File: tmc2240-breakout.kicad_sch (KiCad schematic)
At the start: 91 parts, among them J1 Conn_01x06, J2 Conn_01x05, J3 Conn_01x02, J4 Conn_01x02, J5 Conn_01x15, J6 Conn_01x06, J7 Conn_01x05, Q10 2N7002, Q11 2N7002, Q12 2N7002, Q13 2N7002, Q14 2N7002, Q2 2N7002, Q3 2N7002, Q5 2N7002, Q6 2N7002, Q7 2N7002, Q8 2N7002, Q9 2N7002, U1 TMC2240ATJ+, U2 LD1117S18TR_SOT223

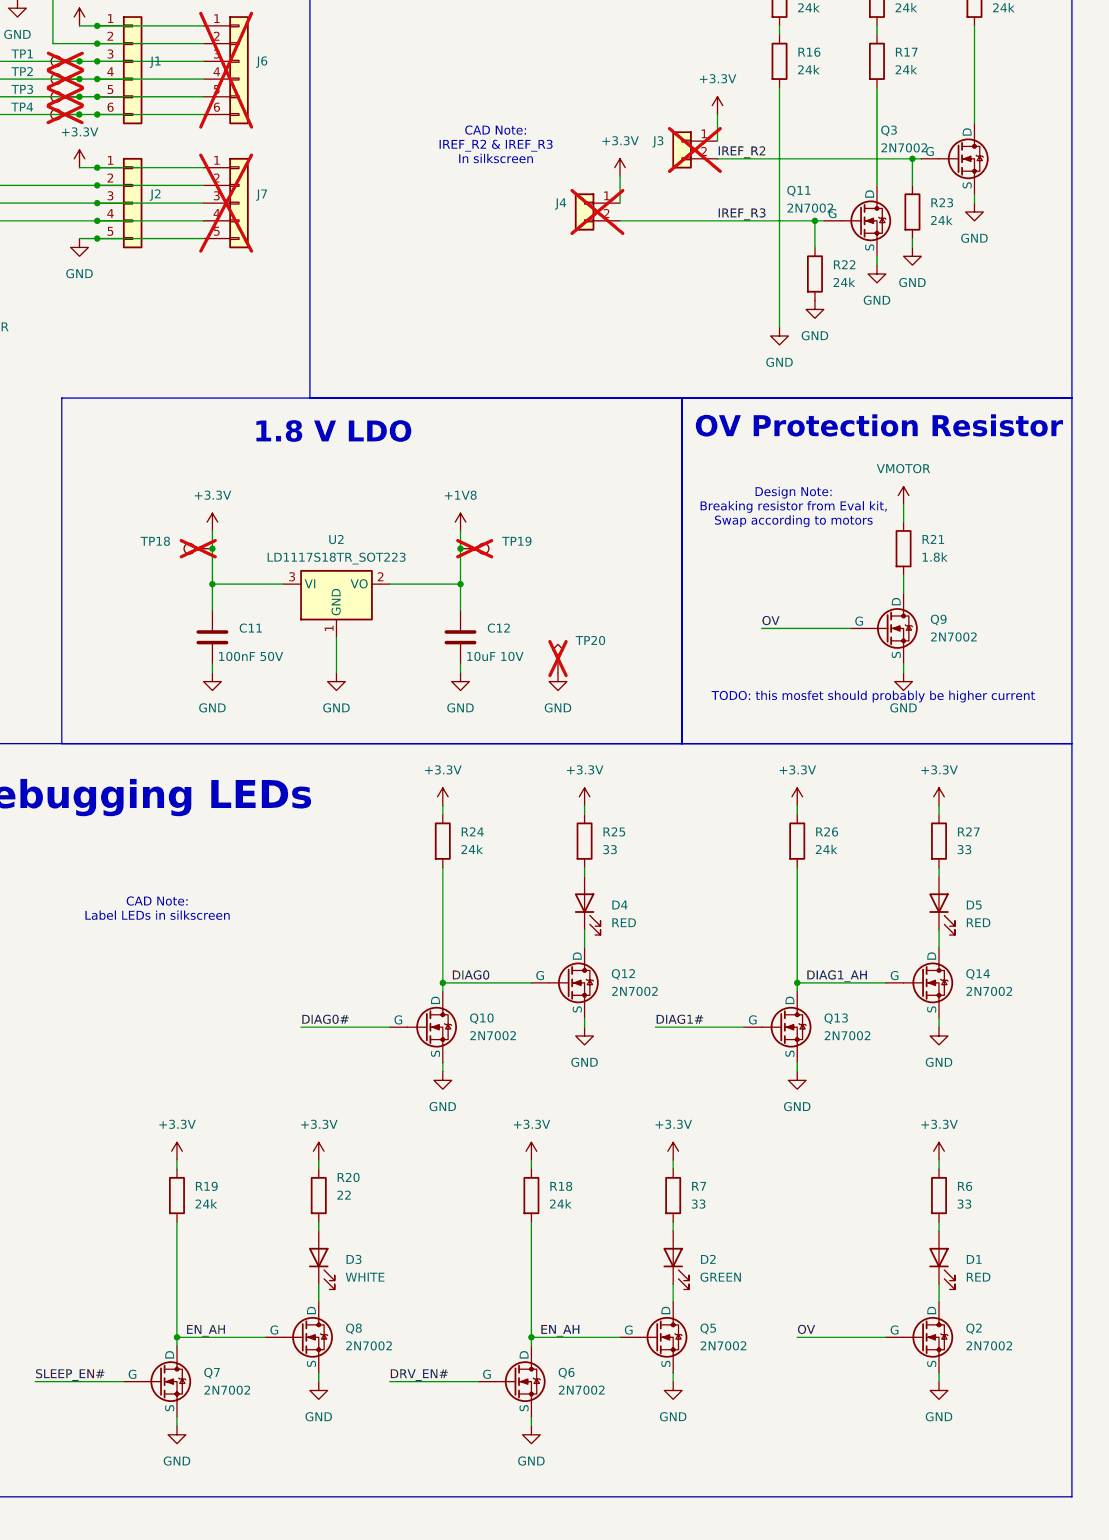
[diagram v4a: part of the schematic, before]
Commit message: did more sourcing and fixed footprints
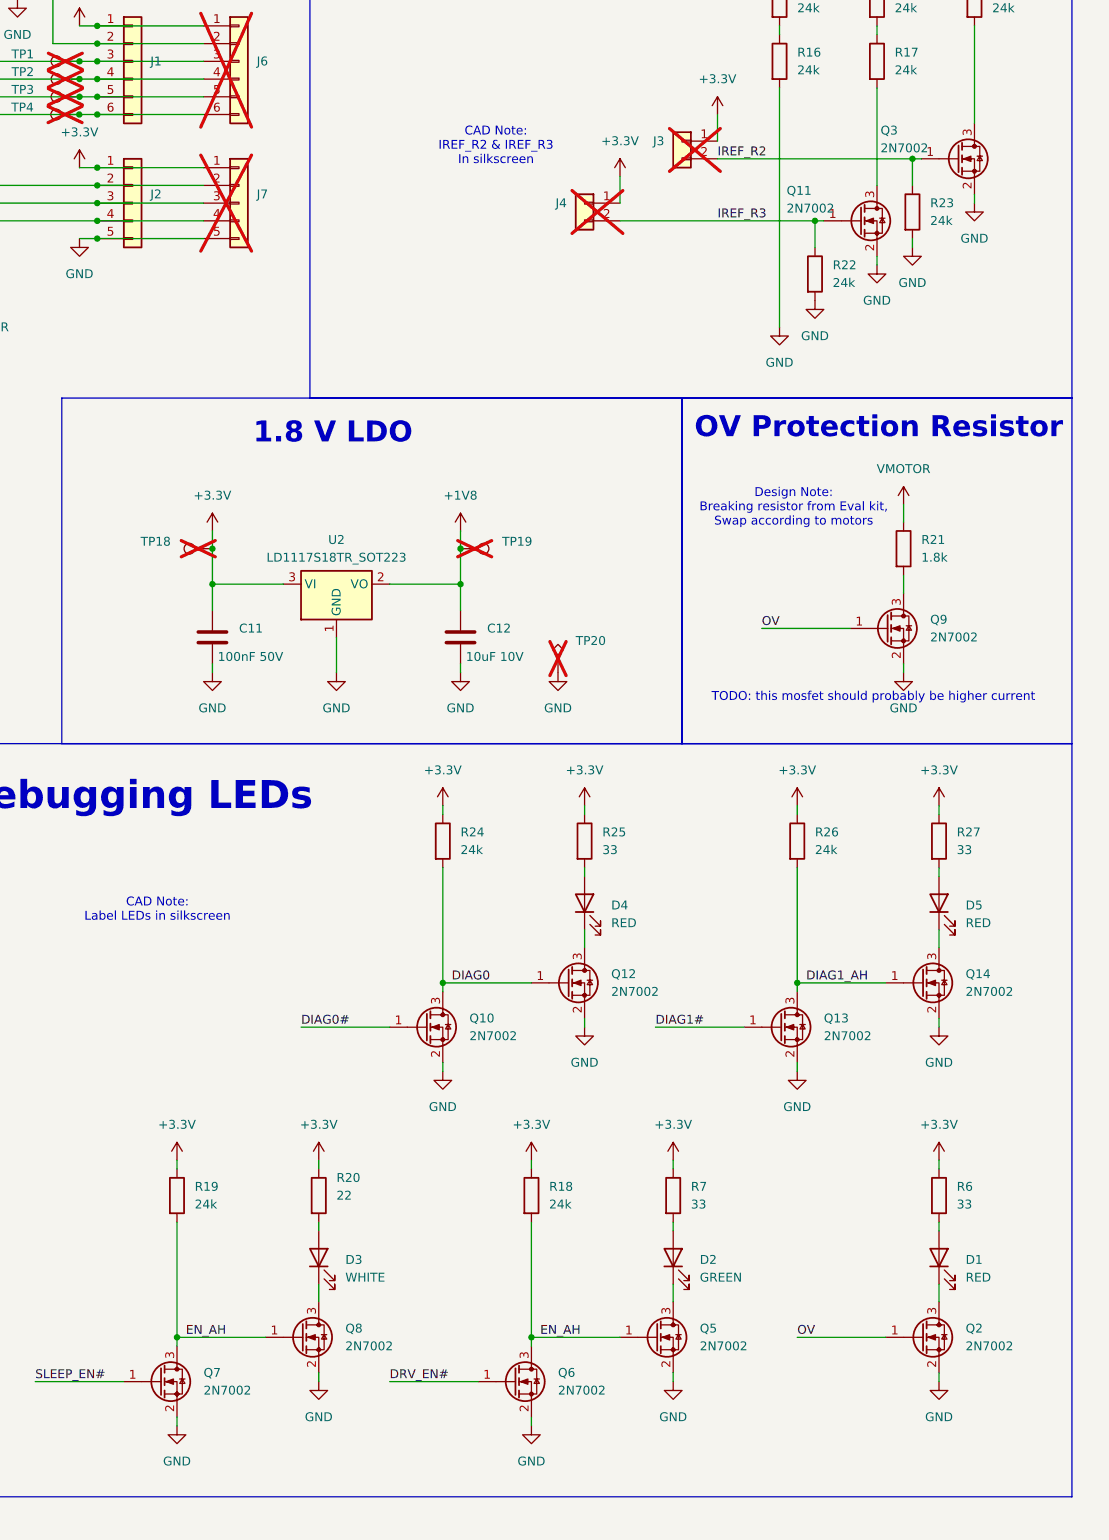
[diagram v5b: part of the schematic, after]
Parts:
- J1: footprint (none) -> XH-W-6A:CONN-TH_6P-P2.50_DEALON_XH-W-6A; LCSC C442330 -> C5160923
- J2: footprint (none) -> HDGC2501WR-5P:CONN-TH_5P-P2.50_HDGC2501WR-5P
- J3, J4: footprint (none) -> Connector_PinHeader_2.54mm:PinHeader_1x02_P2.54mm_Vertical
- J5: footprint (none) -> Connector_PinHeader_2.54mm:PinHeader_1x15_P2.54mm_Vertical
- J6: footprint (none) -> Connector_JST:JST_XH_B6B-XH-A_1x06_P2.50mm_Vertical
- J7: footprint (none) -> Connector_JST:JST_XH_B5B-XH-A_1x05_P2.50mm_Vertical
- Q10, Q11, Q12, Q13, Q14, Q2, Q3, Q5, Q6, Q7, Q8, Q9: footprint (none) -> Package_TO_SOT_SMD:SOT-23; symbol Simulation_SPICE:NMOS -> Transistor_FET:Q_NMOS_GSD
- TP1, TP10, TP11, TP12, TP13, TP14, TP15, TP16, TP17, TP18, TP19, TP2, TP3, TP4, TP5, TP6, TP7, TP8, TP9: footprint (none) -> TestPoint:TestPoint_THTPad_D1.0mm_Drill0.5mm
- TP20, TP21: footprint (none) -> TestPoint:TestPoint_THTPad_1.0x1.0mm_Drill0.5mm
- U1: footprint 21-0140_T3255+5C_TRI -> ul_TMC2240ATJ-:21-0140_T3255&plus_5C_TRI
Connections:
- net DIAG0: now also Q10.3 (D), Q12.1 (G); no longer Q10.1 (D), Q12.2 (G)
- net DIAG0#: now also Q10.1 (G); no longer Q10.2 (G)
- net DIAG1#: now also Q13.1 (G); no longer Q13.2 (G)
- net DIAG1_AH: now also Q13.3 (D), Q14.1 (G); no longer Q13.1 (D), Q14.2 (G)
- net DRV_EN#: now also Q6.1 (G); no longer Q6.2 (G)
- net EN_AH: now also Q5.1 (G), Q6.3 (D), Q7.3 (D), Q8.1 (G); no longer Q5.2 (G), Q6.1 (D), Q7.1 (D), Q8.2 (G)
- net GND: now also Q10.2 (S), Q11.2 (S), Q12.2 (S), Q13.2 (S), Q14.2 (S), Q2.2 (S), Q3.2 (S), Q5.2 (S), Q6.2 (S), Q7.2 (S), Q8.2 (S), Q9.2 (S); no longer Q10.3 (S), Q11.3 (S), Q12.3 (S), Q13.3 (S), Q14.3 (S), Q2.3 (S), Q3.3 (S), Q5.3 (S), Q6.3 (S), Q7.3 (S), Q8.3 (S), Q9.3 (S)
- net IREF_R2: now also Q3.1 (G); no longer Q3.2 (G)
- net IREF_R3: now also Q11.1 (G); no longer Q11.2 (G)
- net OV: now also Q2.1 (G), Q9.1 (G); no longer Q2.2 (G), Q9.2 (G)
- net SLEEP_EN#: now also Q7.1 (G); no longer Q7.2 (G)
- net at D4.1 (K): now also Q12.3 (D); no longer Q12.1 (D)
- net at R21.2: now also Q9.3 (D); no longer Q9.1 (D)
- net at R15.2: now also Q3.3 (D); no longer Q3.1 (D)
- net at R17.2: now also Q11.3 (D); no longer Q11.1 (D)
- net at D5.1 (K): now also Q14.3 (D); no longer Q14.1 (D)
- net at D2.1 (K): now also Q5.3 (D); no longer Q5.1 (D)
- net at D1.1 (K): now also Q2.3 (D); no longer Q2.1 (D)
- net at D3.1 (K): now also Q8.3 (D); no longer Q8.1 (D)

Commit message: did some pcb placement
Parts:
- added J8: Conn_01x02, TerminalBlock_Phoenix:TerminalBlock_Phoenix_MKDS-1,5-2_1x02_P5.00mm_Horizontal, symbol Connector_Generic:Conn_01x02
- J5: value Conn_01x15 -> Conn_01x17; footprint Connector_PinHeader_2.54mm:PinHeader_1x15_P2.54mm_Vertical -> Connector_PinHeader_2.54mm:PinHeader_1x17_P2.54mm_Vertical; symbol Connector_Generic:Conn_01x15 -> Connector_Generic:Conn_01x17; now in the parts list
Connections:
- net +3.3V: now also J5.17 (Pin_17)
- net DIAG0#: now also J5.12 (Pin_12); no longer J5.11 (Pin_11)
- net DIAG1#: now also J5.13 (Pin_13); no longer J5.12 (Pin_12)
- net DIR: now also J5.7 (Pin_7); no longer J5.6 (Pin_6)
- net DRV_EN#: now also J5.8 (Pin_8); no longer J5.7 (Pin_7)
- net EN_AH: no longer Q7.3 (D), Q8.1 (G), R19.2
- net GND: now also J5.1 (Pin_1), J8.1 (Pin_1)
- net IREF: now also J5.14 (Pin_14); no longer J5.13 (Pin_13)
- net IREF_R2: now also J5.15 (Pin_15); no longer J5.14 (Pin_14)
- net IREF_R3: now also J5.16 (Pin_16); no longer J5.15 (Pin_15)
- net OV: now also J5.9 (Pin_9); no longer J5.8 (Pin_8)
- net SLEEP#: now also J5.11 (Pin_11); no longer J5.10 (Pin_10)
- net SPI_CS#: now also J5.5 (Pin_5); no longer J5.4 (Pin_4)
- net SPI_SCK: now also J5.2 (Pin_2); no longer J5.1 (Pin_1)
- net SPI_SDI: now also J5.3 (Pin_3); no longer J5.2 (Pin_2)
- net SPI_SDO: now also J5.4 (Pin_4); no longer J5.3 (Pin_3)
- net STEP: now also J5.6 (Pin_6); no longer J5.5 (Pin_5)
- net UART_EN: now also J5.10 (Pin_10); no longer J5.9 (Pin_9)
- net VMOTOR: now also J8.2 (Pin_2)
- net DIAG0 renamed DIAG0_AH
- new net SLEEP_AH: Q7.3 (D), Q8.1 (G), R19.2

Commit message: started doing some routing
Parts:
- U1: footprint ul_TMC2240ATJ-:21-0140_T3255&plus_5C_TRI -> 21-0140_T3255+5C_TRI
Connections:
- net SLEEP_EN# is gone; now on net SLEEP#: Q7.1 (G)
- net DIR: now also J5.8 (Pin_8), TP11.1; no longer J5.7 (Pin_7), TP10.1
- net DRV_EN#: now also J5.10 (Pin_10), TP13.1; no longer J5.8 (Pin_8), TP11.1
- net IREF: now also J5.9 (Pin_9), TP12.1; no longer J5.14 (Pin_14), TP17.1
- net OUT1A: now also J1.6 (Pin_6), J6.6 (Pin_6), TP4.1; no longer J1.3 (Pin_3), J6.3 (Pin_3), TP1.1
- net OUT1B: now also J1.3 (Pin_3), J6.3 (Pin_3), TP1.1; no longer J1.4 (Pin_4), J6.4 (Pin_4), TP2.1
- net OUT2B: now also J1.4 (Pin_4), J6.4 (Pin_4), TP2.1; no longer J1.6 (Pin_6), J6.6 (Pin_6), TP4.1
- net OV: now also J5.14 (Pin_14), TP17.1; no longer J5.9 (Pin_9), TP12.1
- net SLEEP#: now also J5.2 (Pin_2), TP5.1; no longer J5.11 (Pin_11), TP14.1
- net SPI_CS#: now also J5.3 (Pin_3), TP6.1; no longer J5.5 (Pin_5), TP8.1
- net SPI_SCK: now also J5.4 (Pin_4), TP7.1; no longer J5.2 (Pin_2), TP5.1
- net SPI_SDI: now also J5.5 (Pin_5), TP8.1; no longer J5.3 (Pin_3), TP6.1
- net SPI_SDO: now also J5.6 (Pin_6), TP9.1; no longer J5.4 (Pin_4), TP7.1
- net STEP: now also J5.7 (Pin_7), TP10.1; no longer J5.6 (Pin_6), TP9.1
- net UART_EN: now also J5.11 (Pin_11), TP14.1; no longer J5.10 (Pin_10), TP13.1
- net CLK: now reaches R4.1, U1.30 (CLK)
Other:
- moved on the sheet: J5, R4, TP10, TP11, TP12, TP13, TP14, TP17, TP5, TP6, TP7, TP8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

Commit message: more pcb layouting
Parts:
- U1: footprint ul_TMC2240ATJ-:21-0140_T3255&plus_5C_TRI -> 21-0140_T3255+5C_TRI
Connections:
- net ENCA: now also J2.4 (Pin_4), J7.4 (Pin_4), R1.1; no longer J2.2 (Pin_2), J7.2 (Pin_2), R3.1
- net ENCN: now also J2.2 (Pin_2), J7.2 (Pin_2), R3.1; no longer J2.4 (Pin_4), J7.4 (Pin_4), R1.1
- net OV_D: now reaches Q9.3 (D), R21.2
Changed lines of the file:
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@@
 		)
 	)
-	(label "ENCA"
-		(at 245.11 64.77 0)
-		(effects
-			(font
-				(size 1.27 1.27)
-			)
-			(justify left bottom)
-		)
-	)
 	(label "DIAG1#"
 		(at 138.43 114.3 0)
@@
 		)
 	)
-	(label "ENCN"
-		(at 245.11 69.85 0)
-		(effects
-			(font
-				(size 1.27 1.27)
-			)
-			(justify left bottom)
-		)
-	)
 	(label "DIAG1#"
 		(at 347.98 185.42 0)
@@
 		)
 	)
+	(label "OV_D"
+		(at 383.54 123.19 0)
+		(effects
+			(font
+				(size 1.27 1.27)
+			)
+			(justify left bottom)
+		)
+	)
 	(label "SPI_SDI"
 		(at 138.43 49.53 0)
@@
 		)
 	)
+	(label "ENCA"
+		(at 245.11 69.85 0)
+		(effects
+			(font
+				(size 1.27 1.27)
+			)
+			(justify left bottom)
+		)
+	)
+	(label "ENCN"
+		(at 245.11 64.77 0)
+		(effects
+			(font
+				(size 1.27 1.27)
+			)
+			(justify left bottom)
+		)
+	)
 	(label "UART_EN"
 		(at 44.45 68.58 180)
@@
 			)
 		)
-		(property "Footprint" "ul_TMC2240ATJ-:21-0140_T3255&plus_5C_TRI"
+		(property "Footprint" "21-0140_T3255+5C_TRI"
 			(at 146.05 245.11 0)
 			(effects
